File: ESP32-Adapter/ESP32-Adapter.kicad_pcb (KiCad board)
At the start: 2 copper layers, 15 parts, among them J1 Conn_01x08_Pin, J10 Barrel_Jack, J12 Conn_01x05, J13 Conn_01x05, J14 Conn_01x04, J2 Conn_01x03, J3 Conn_01x03, U1 ESP32-C5-DevKitC-1, U2 LM317_TO-263, U3 Adafruit CANPAL

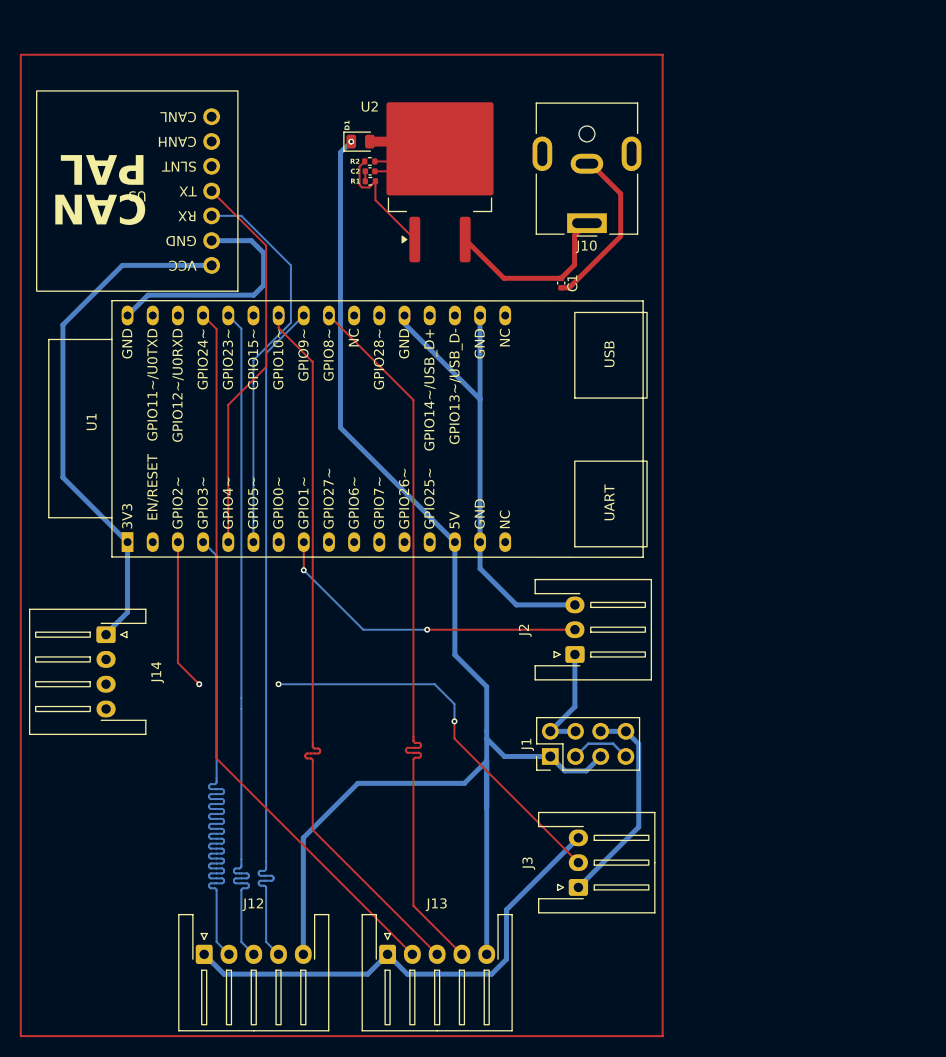
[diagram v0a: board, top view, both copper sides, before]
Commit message: finish general routing of board
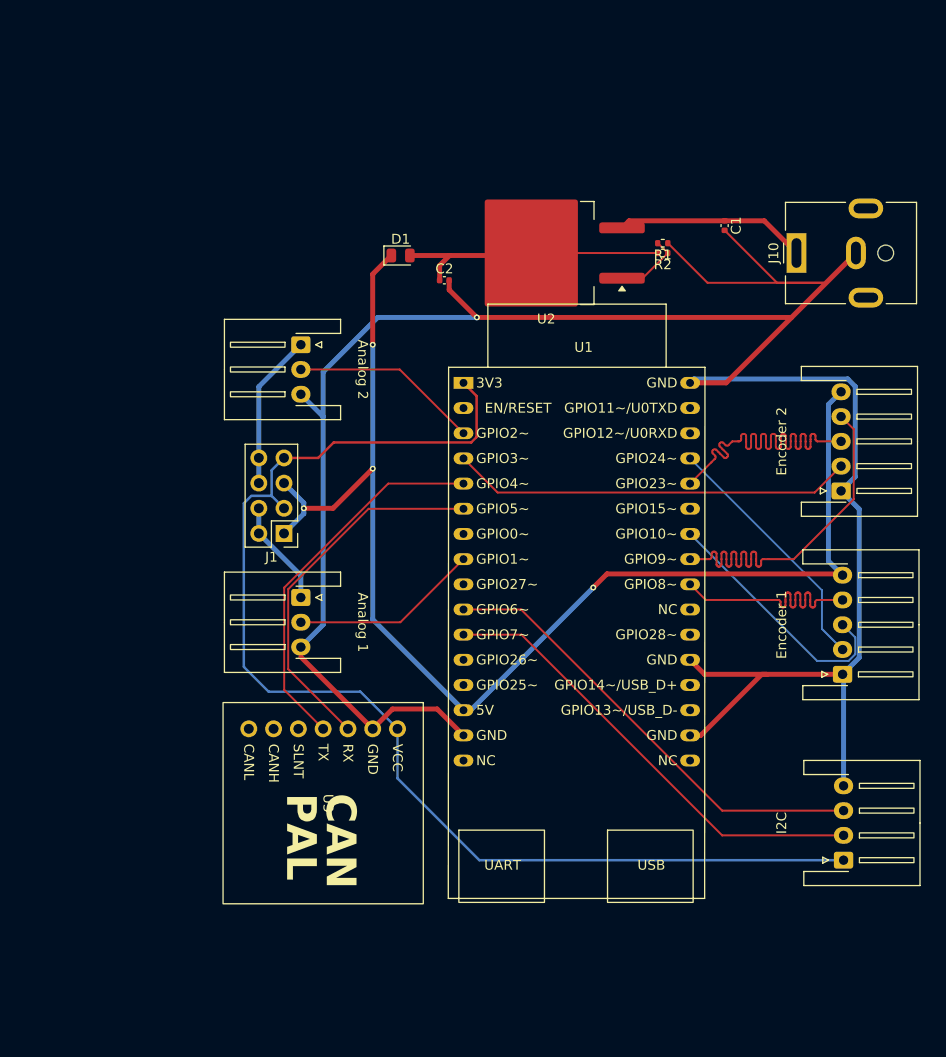
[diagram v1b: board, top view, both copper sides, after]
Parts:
- moved J12 79.5 mm to (142.2, 73.0), turned to 90 degrees
- moved J14 77.8 mm to (142.5, 110.2), turned to 90 degrees
- moved U3 64.5 mm to (90.0, 104.5), turned to -90 degrees
- moved J3 61.5 mm to (87.8, 58.2), turned to -90 degrees
- moved J13 53.9 mm to (142.4, 91.5), turned to 90 degrees
- moved U1 37.5 mm to (104.1, 62.1), turned to 0 degrees
- moved J1 35.0 mm to (86.0, 77.3), turned to 180 degrees
- moved R2 31.0 mm to (124.3, 49.0), turned to 180 degrees
- moved R1 30.2 mm to (124.3, 48.0), turned to 180 degrees
- moved J2 28.2 mm to (87.8, 83.8), turned to -90 degrees
- moved J10 21.4 mm to (137.8, 49.0), turned to 90 degrees
- moved C1 17.5 mm to (130.5, 46.2)
- moved U2 14.0 mm to (112.5, 49.0), turned to 180 degrees
- moved C2 13.3 mm to (102.2, 51.8), turned to 0 degrees
- moved D1 12.2 mm to (97.8, 49.2)
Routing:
- net GND: track 139.2 -> 250.9 mm, vias 0 -> 1
- net +3.3V: track 58.5 -> 123.6 mm
- net /IDX1: track 73.8 -> 25.0 mm
- net /A1: track 73.6 -> 25.8 mm
- net /B1: track 73.2 -> 25.7 mm
- net /I2C SDA: track 0.00 -> 46.7 mm
- net /I2C SCL: track 0.00 -> 46.7 mm
- net /SIG2: track 55.0 -> 19.1 mm, vias 3 -> 0
- net /A2: track 70.6 -> 40.2 mm
- net /IDX2: track 70.3 -> 40.8 mm
- net /B2: track 70.0 -> 40.6 mm
- net /SIG1: track 32.9 -> 19.2 mm, vias 2 -> 0
- net +5V: track 140.9 -> 129.4 mm, vias 1 -> 4
- net Net-(J1-Pin_6): track 21.4 -> 15.7 mm
- net Net-(U2-ADJ): track 12.1 -> 7.10 mm
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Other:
- board text added: "Analog 1"
- board text added: "Analog 2"
- board text added: "Encoder 1"
- board text added: "Encoder 2"
- board text added: "GPIO8~"
- board text added: "I2C"

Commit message: add board outline and mounting holes
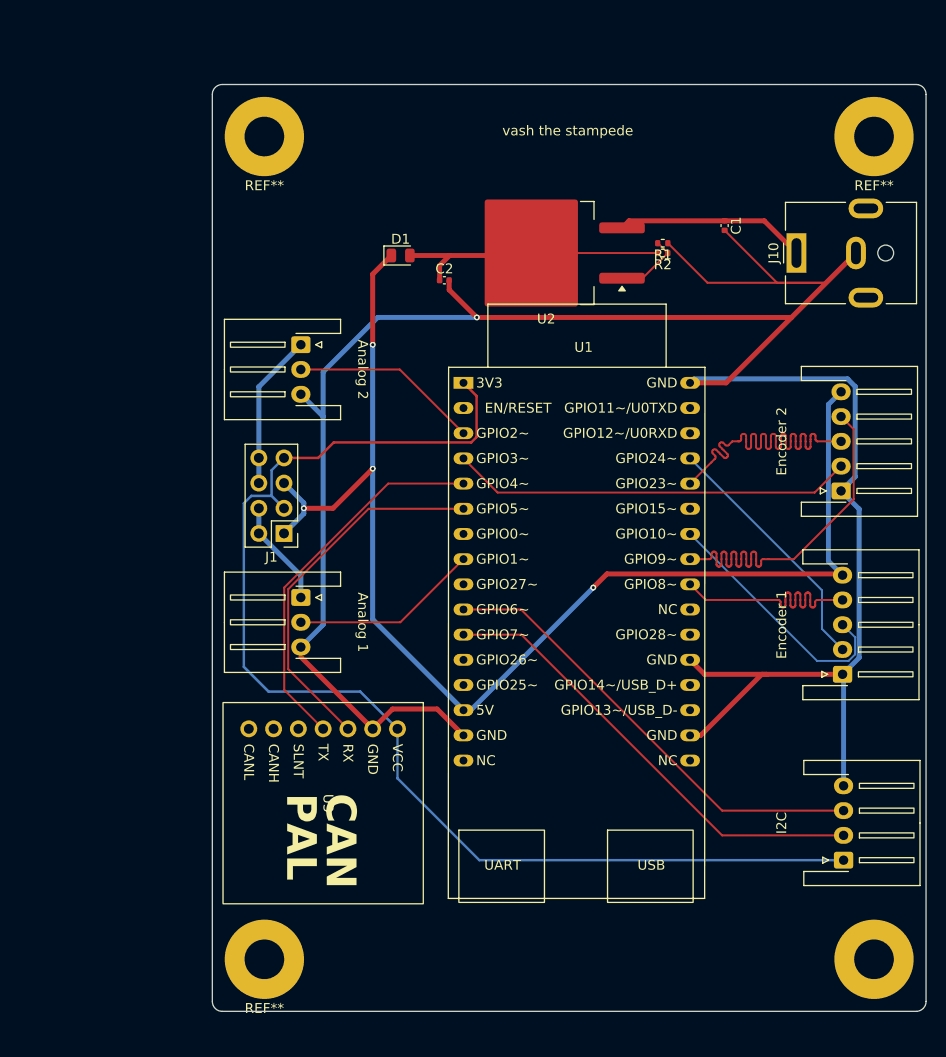
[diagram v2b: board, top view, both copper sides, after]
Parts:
- added ?: , , F.Cu at (145.6, 120.2)
- added REF**: MountingHole_4mm_Pad, MountingHole:MountingHole_4mm_Pad, F.Cu at (84.1, 37.2)
- added REF**: MountingHole_4mm_Pad, MountingHole:MountingHole_4mm_Pad, F.Cu at (145.6, 37.2)
- added REF**: MountingHole_4mm_Pad, MountingHole:MountingHole_4mm_Pad, F.Cu at (84.1, 120.2)
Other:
- board outline added: 72 x 93.5 mm
- board text added: "vash the stampede"

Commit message: add mars logo and vash the stampede art
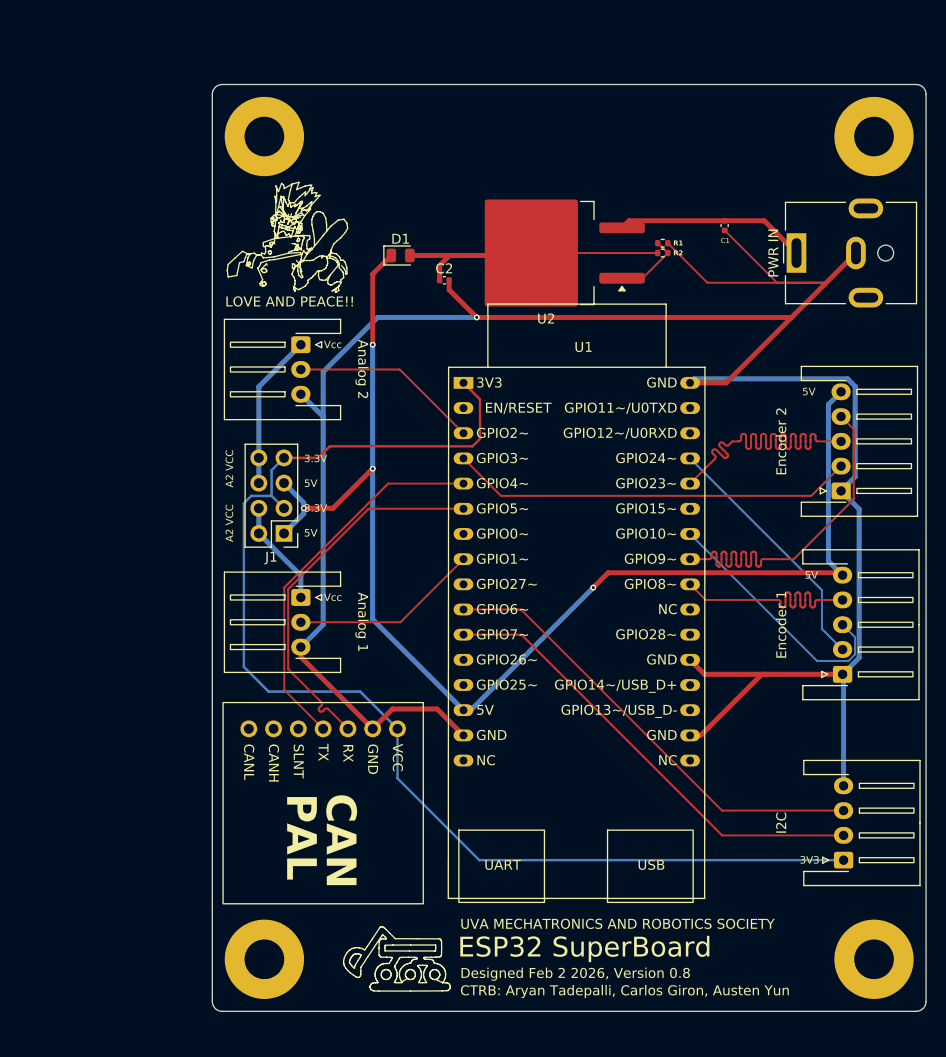
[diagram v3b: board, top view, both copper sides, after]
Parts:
- PWR IN: renamed from J10
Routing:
- net /CAN RX: track 37.6 -> 38.7 mm
- net +3.3V: track 123.6 -> 124.1 mm
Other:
- board text added: "3.3V"
- board text added: "3V3"
- board text added: "5V"
- board text added: "A2 VCC"
- board text added: "CTRB: Aryan Tadepalli, Carlos Giron, Austen Yun"
- board text added: "Designed Feb 2 2026, Version 0.8"
- board text added: "ESP32 SuperBoard"
- board text added: "LOVE AND PEACE!!"
- board text added: "UVA MECHATRONICS AND ROBOTICS SOCIETY"
- board text added: "Vcc"
- board text removed: "vash the stampede"

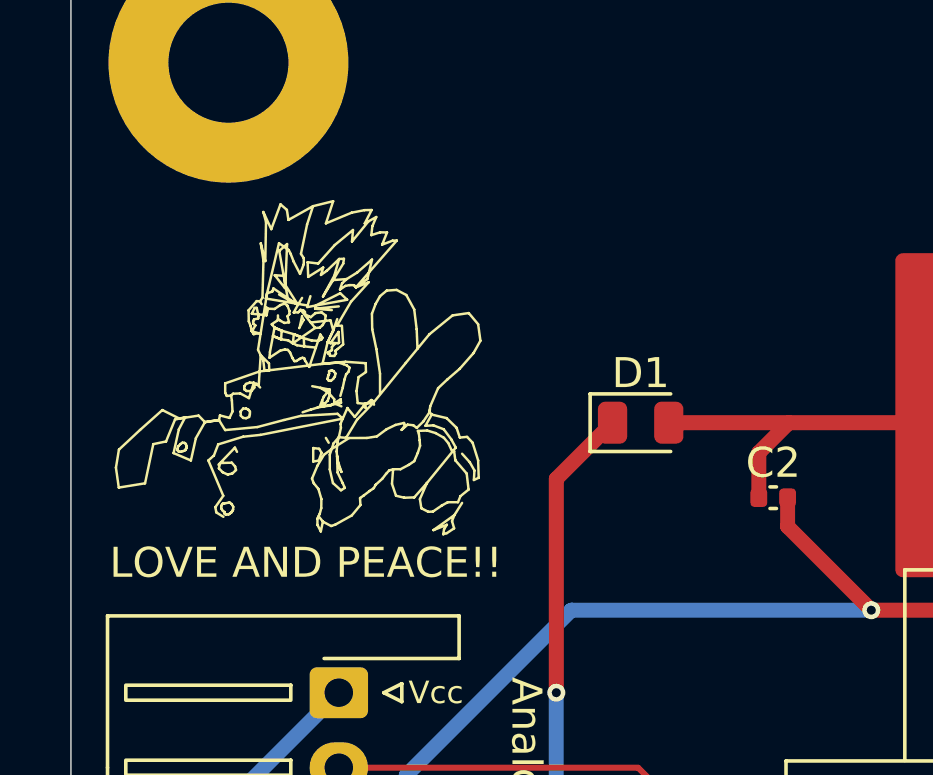
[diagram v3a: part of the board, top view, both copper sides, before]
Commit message: fix small layout error
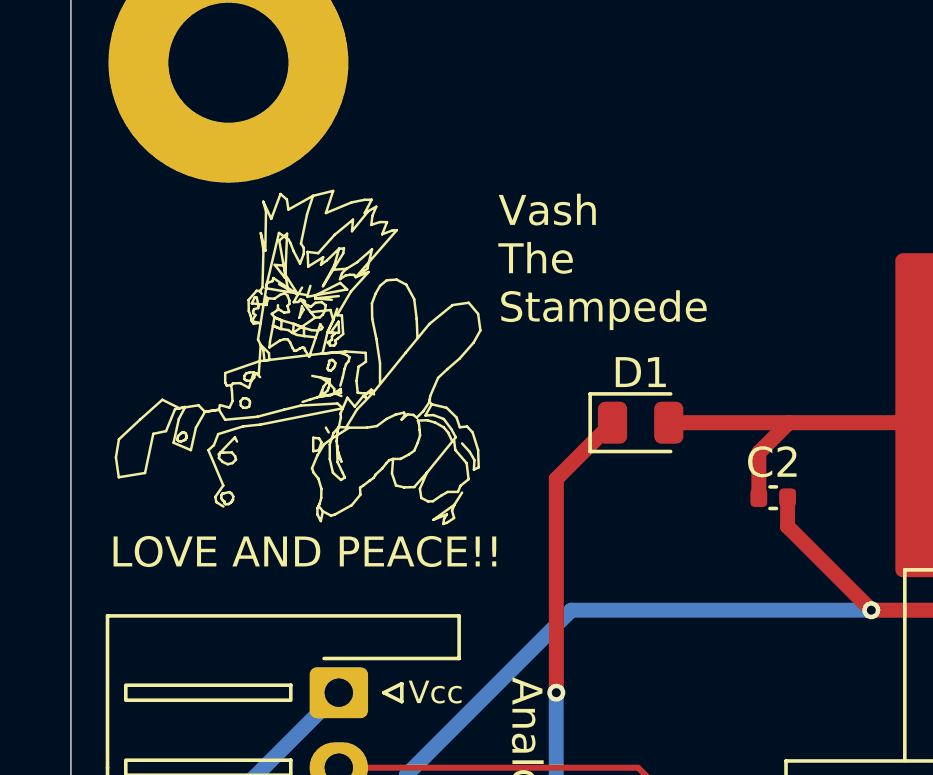
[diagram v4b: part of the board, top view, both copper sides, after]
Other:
- board text added: "Vash The Stampede"

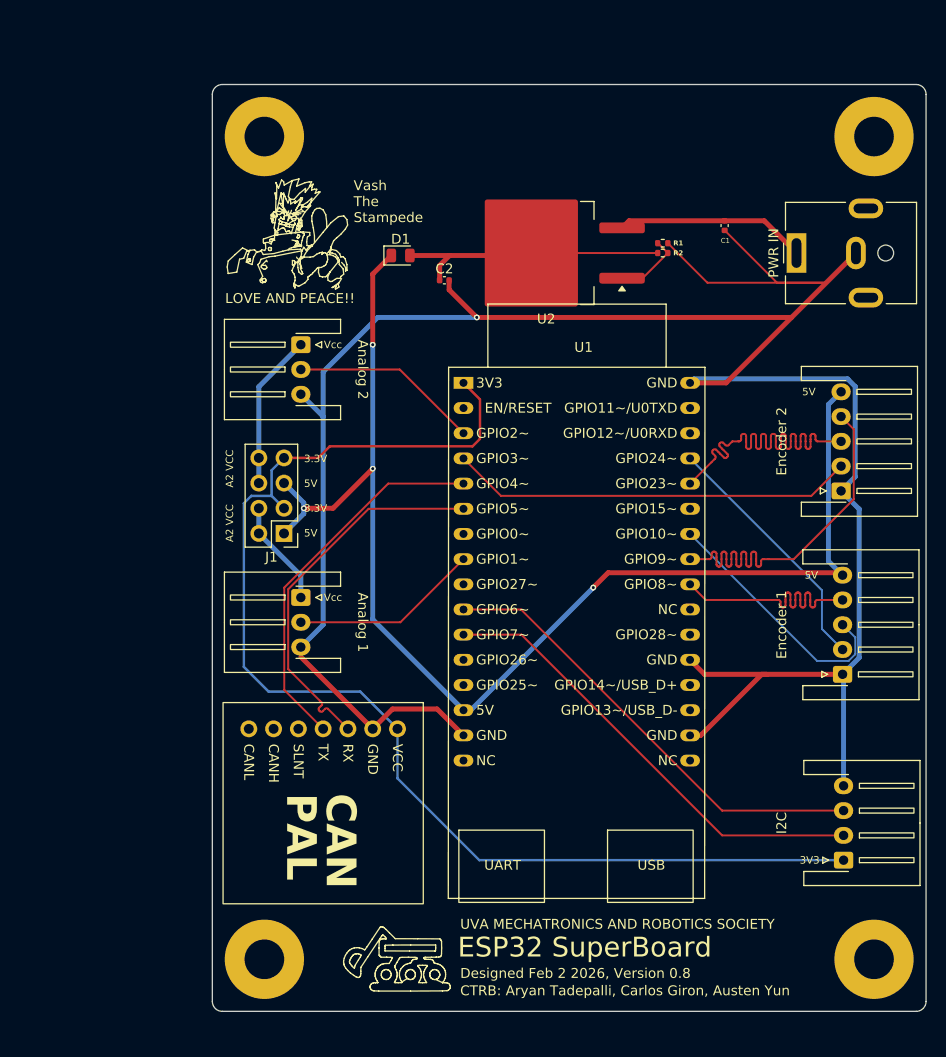
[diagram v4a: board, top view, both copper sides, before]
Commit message: turn canpal to not face screw
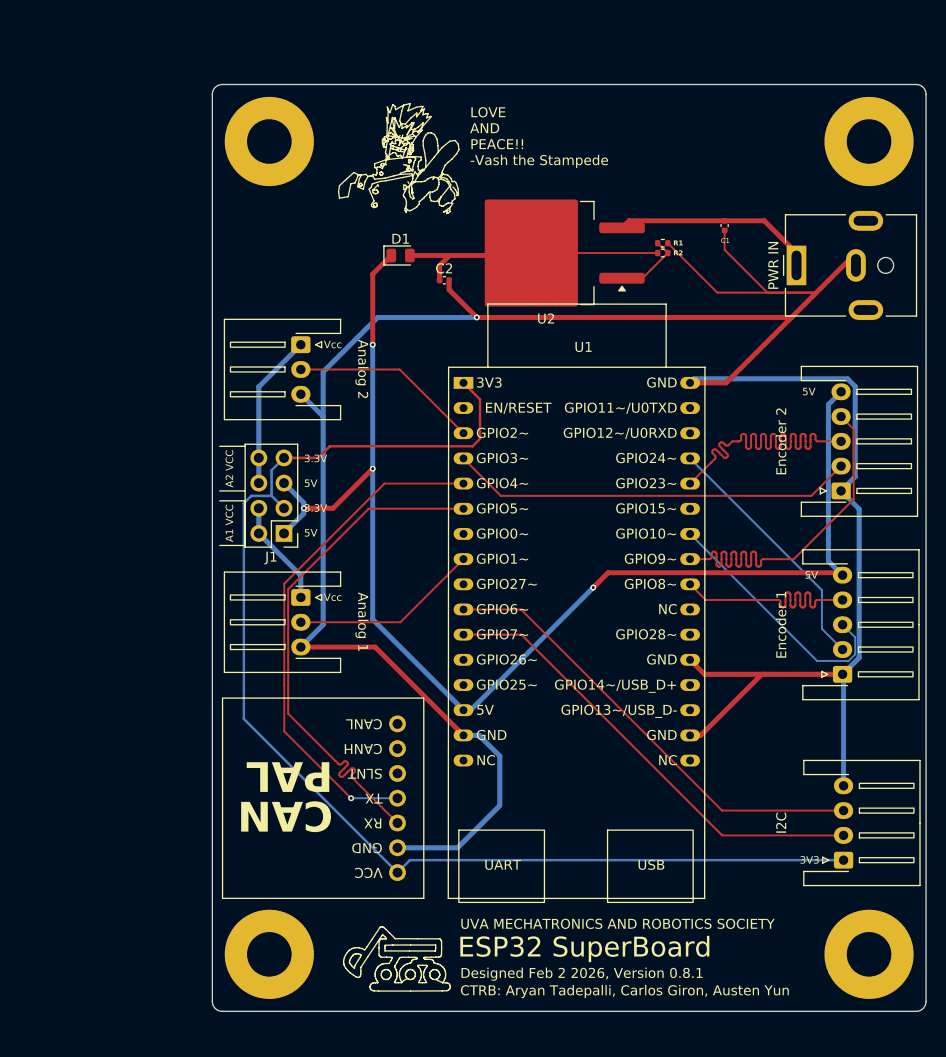
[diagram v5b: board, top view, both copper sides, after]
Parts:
- removed the ? at (145.6, 120.2)
- removed the REF** at (84.1, 37.2)
- removed the REF** at (145.6, 37.2)
- removed the REF** at (84.1, 120.2)
- added ?: , , F.Cu at (145.1, 37.8)
- added ?: , , F.Cu at (145.1, 119.8)
- added ?: , , F.Cu at (84.6, 119.8)
- added REF**: MountingHole_4.5mm_Pad, MountingHole:MountingHole_4.5mm_Pad, F.Cu at (84.6, 37.8)
- moved PWR IN 1.25 mm to (137.8, 50.2)
- moved U3 0.50 mm to (90.0, 104.0), turned to 180 degrees
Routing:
- net GND: track 250.9 -> 272.2 mm
- net /CAN RX: track 38.7 -> 52.9 mm
- net /CAN TX: track 38.3 -> 51.4 mm, vias 0 -> 1
- net +3.3V: track 124.1 -> 125.3 mm
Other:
- board text added: "A1 VCC"
- board text added: "Designed Feb 2 2026, Version 0.8.1"
- board text added: "LOVE AND PEACE!! -Vash the Stampede"
- board text removed: "Designed Feb 2 2026, Version 0.8"
- board text removed: "LOVE AND PEACE!!"
- board text removed: "Vash The Stampede"

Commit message: finish first version of neopixel board
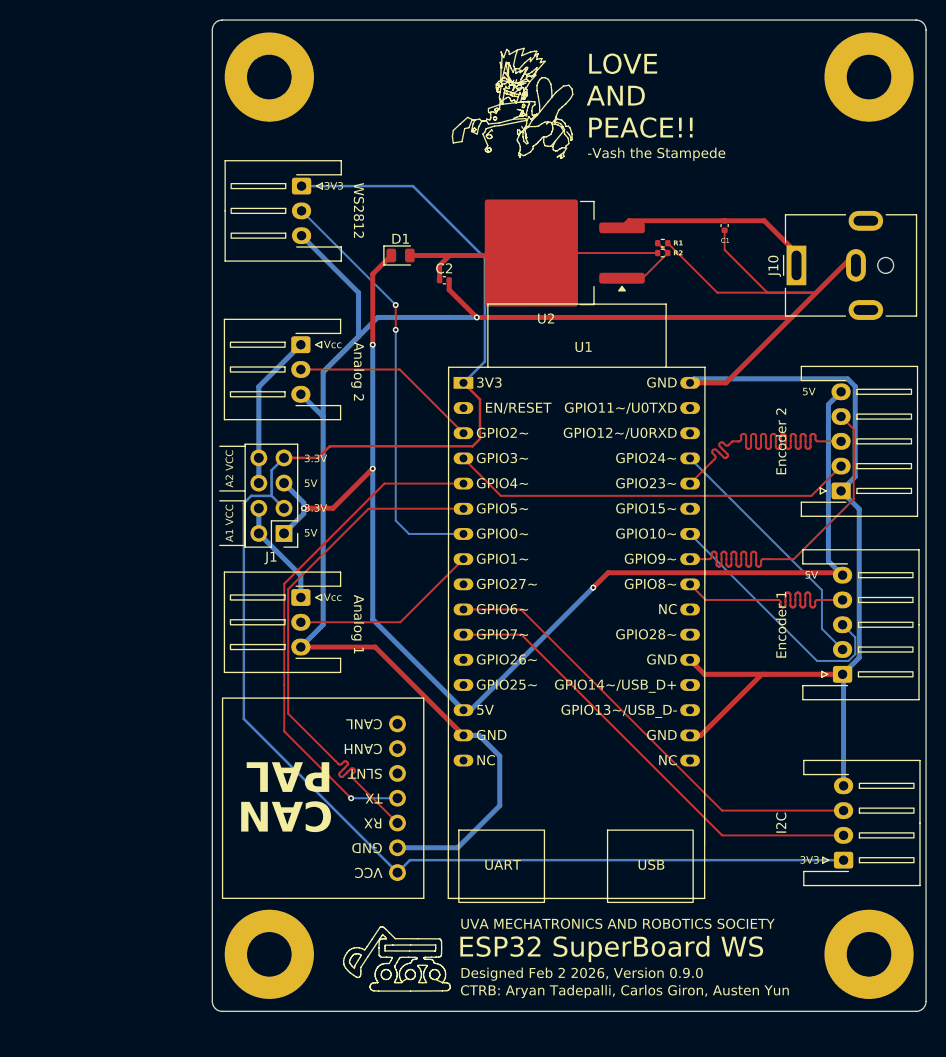
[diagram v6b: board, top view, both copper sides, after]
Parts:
- added J5: Conn_01x03, Connector_JST:JST_XH_S3B-XH-A-1_1x03_P2.50mm_Horizontal, F.Cu at (87.8, 42.2)
- J10: renamed from PWR IN
- moved ? 6.50 mm to (145.1, 31.2)
- moved REF** 6.50 mm to (84.6, 31.2)
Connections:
- U1 pad 7: unconnected-(U1-GPIO0-Pad7) -> /WS2812
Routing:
- net /WS2812: track 0.00 -> 42.6 mm, vias 0 -> 2
- net +3.3V: track 125.3 -> 160.3 mm
- net GND: track 272.2 -> 289.6 mm
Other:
- board size 72 x 93.5 mm -> 72 x 100 mm
- board text added: "-Vash the Stampede"
- board text added: "Designed Feb 2 2026, Version 0.9.0"
- board text added: "ESP32 SuperBoard WS"
- board text added: "LOVE AND PEACE!!"
- board text added: "WS2812"
- board text removed: "Designed Feb 2 2026, Version 0.8.1"
- board text removed: "ESP32 SuperBoard"
- board text removed: "LOVE AND PEACE!! -Vash the Stampede"
